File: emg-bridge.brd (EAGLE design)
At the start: 98.7 x 40.6 mm, 23 parts

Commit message: Updated parts from eagle-lib. Worked out pinouts for all connectors.
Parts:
- removed U$3: STEWART_SS-666604-NF, eagle-lib:STEWART_SS-666604-NF
- removed U$4: TE_640389-3, eagle-lib:TE_640389-3
- added J1, J2: RJ25_4X1, eagle-lib:RJ25_4X1
- U$1: value STEWART_SS-666604-NF -> M03_0.156IN-RA; device eagle-lib:STEWART_SS-666604-NF -> eagle-lib:TE_640389-3
- moved JP2 58.6 mm to (68.6, 31.8), turned to 0 degrees
- moved U$1 53.6 mm to (55.9, 15.2), turned to 180 degrees
- moved U$2 5.68 mm to (57.1, 31.8)
- moved C2 5.08 mm to (61.0, 25.4)
- moved C1 4.02 mm to (57.1, 38.1)
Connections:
- new net +VE: JP2.1, R1.2, R11.2, R13.2, R15.2, R3.2, R5.2, R7.2, R9.2, U$2.8
- new net -VE: C2.1, R10.2, R12.2, R14.2, R16.2, R2.2, R4.2, R6.2, R8.2, U$2.5
- new net CH1: J1.P$4, JP2.3
- new net CH2: J1.P$10, JP2.4
- new net CH3: J1.P$16, JP2.5
- new net CH4: J1.P$22, JP2.6
- new net CH5: J2.P$4, JP2.7
- new net CH6: J2.P$10, JP2.8
- new net CH7: J2.P$16, JP2.9
- new net CH8: J2.P$22, JP2.10
- new net GND: C2.2, J1.P$11, J1.P$14, J1.P$17, J1.P$2, J1.P$20, J1.P$23, J1.P$5, J1.P$8, J2.P$11, J2.P$14, J2.P$17, J2.P$2, J2.P$20, J2.P$23, J2.P$5, J2.P$8, JP2.2, U$1.P$2, U$2.3, U$2.6
- new net N$1: J1.P$1, R2.1
- new net N$11: J1.P$13, R6.1
- new net N$13: J1.P$15, R5.1
- new net N$16: J1.P$19, R8.1
- new net N$18: J1.P$21, R7.1
- new net N$2: C1.2, U$2.4
- new net N$21: J2.P$1, R10.1
- new net N$23: J2.P$3, R9.1
- new net N$26: J2.P$7, R12.1
- new net N$28: J2.P$9, R11.1
- new net N$3: J1.P$3, R1.1
- new net N$31: J2.P$13, R14.1
- new net N$33: J2.P$15, R13.1
- new net N$36: J2.P$19, R16.1
- new net N$38: J2.P$21, R15.1
- new net N$4: C1.1, U$2.2
- new net N$6: J1.P$7, R4.1
- new net N$8: J1.P$9, R3.1

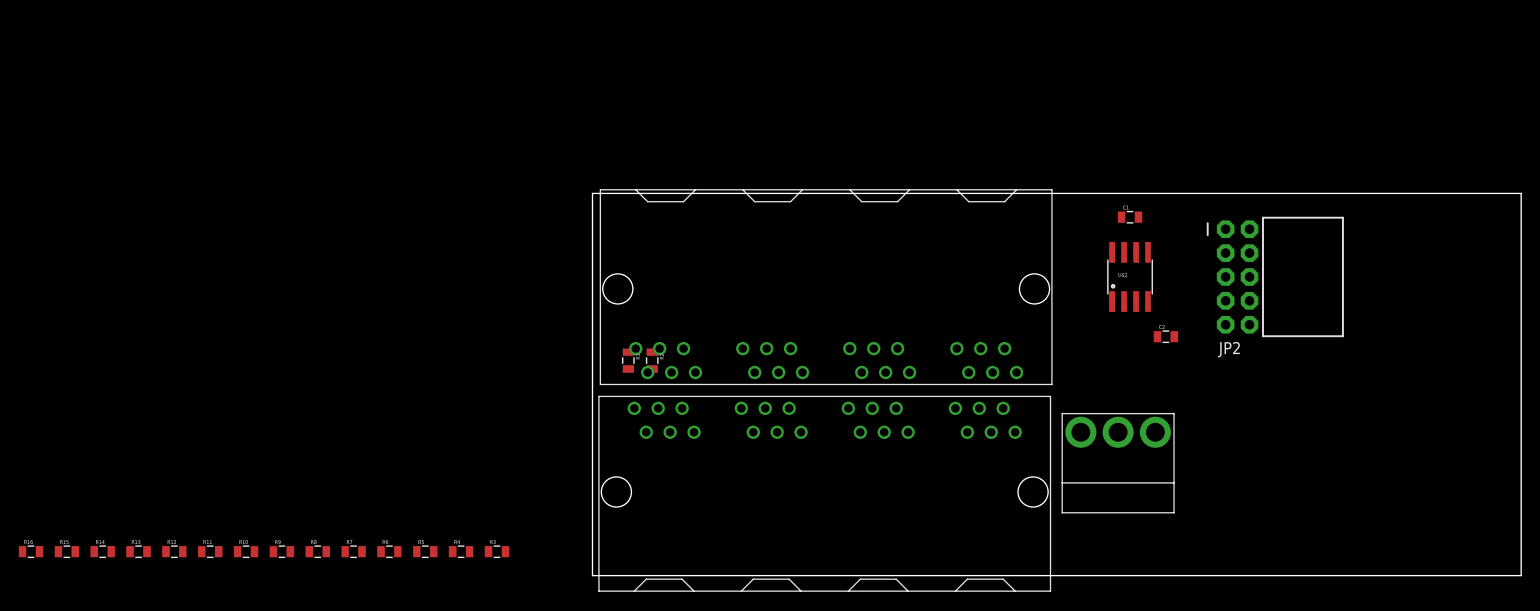
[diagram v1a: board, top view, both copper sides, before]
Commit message: Schematic cleaned up and board layout/routing rough draft completed.
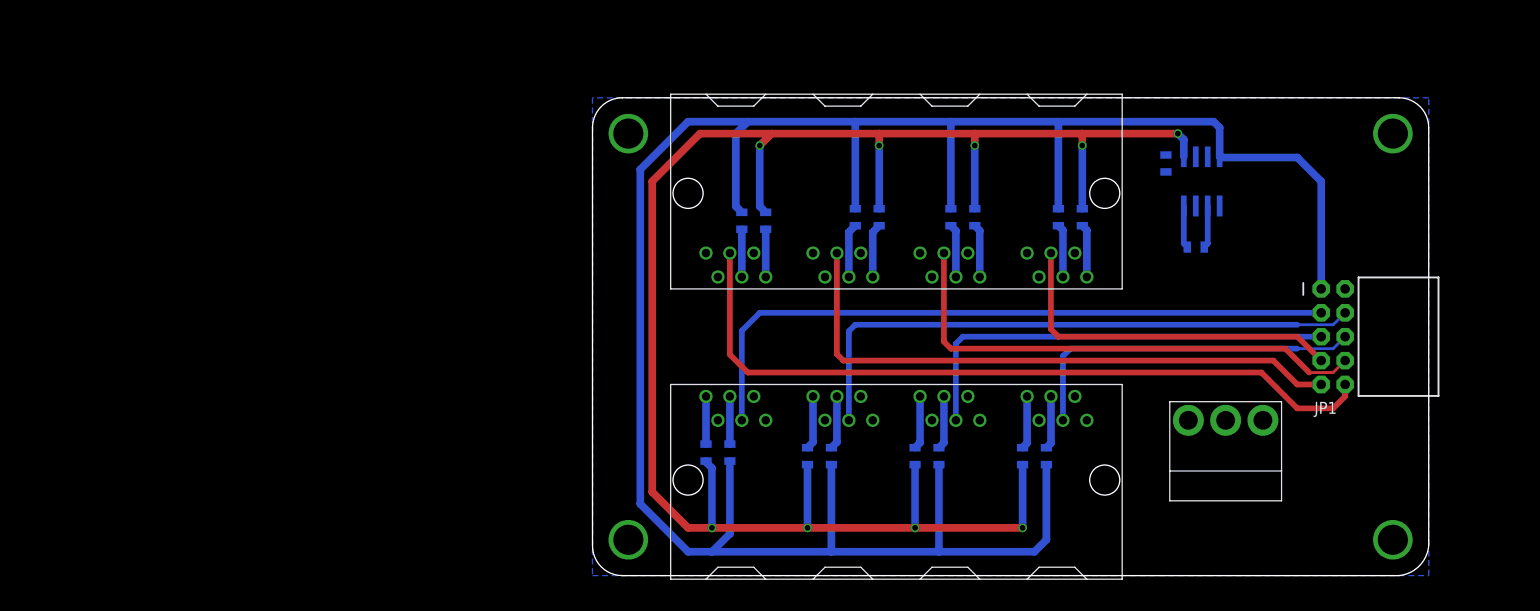
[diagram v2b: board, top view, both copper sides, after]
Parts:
- removed JP2: M05X2RAF, SparkFun-Connectors:2X5-RAF
- removed U$1: M03_0.156IN-RA, eagle-lib:TE_640389-3
- removed U$2: ADM660ARZ, eagle-lib:SOIC8
- added J3: M03_0.156IN-RA, eagle-lib:TE_640389-3
- added JP1: M05X2RAF, SparkFun-Connectors:2X5-RAF
- added U1: ADM660ARZ, eagle-lib:SOIC8
- C1, C2: value (none) -> 10uF
- R1, R10, R11, R12, R13, R14, R15, R16, R2, R3, R4, R5, R6, R7, R8, R9: value (none) -> 100
- moved R10 95.7 mm to (52.1, 38.1), flipped to the bottom, turned to 90 degrees
- moved R12 92.2 mm to (40.6, 38.1), flipped to the bottom, turned to 90 degrees
- moved R9 89.9 mm to (49.5, 38.1), flipped to the bottom, turned to 90 degrees
- moved R14 89.9 mm to (30.5, 38.1), flipped to the bottom, turned to 90 degrees
- moved R11 86.4 mm to (38.1, 38.1), flipped to the bottom, turned to 90 degrees
- moved R16 85.7 mm to (18.4, 37.7), flipped to the bottom, turned to 90 degrees
- moved R13 84.1 mm to (27.9, 38.1), flipped to the bottom, turned to 90 degrees
- moved R15 79.9 mm to (15.9, 37.7), flipped to the bottom, turned to 90 degrees
- moved R8 75.6 mm to (45.7, 12.7), flipped to the bottom, turned to 270 degrees
- moved R7 74.4 mm to (48.3, 12.7), flipped to the bottom, turned to 270 degrees
- moved J2 60.9 mm to (54.5, 40.6), turned to 180 degrees
- moved R6 56.8 mm to (34.3, 12.7), flipped to the bottom, turned to 270 degrees
- moved R5 55.5 mm to (36.8, 12.7), flipped to the bottom, turned to 270 degrees
- moved J1 42.1 mm to (10.2, 10.2), turned to 0 degrees
- moved R4 38.2 mm to (22.9, 12.7), flipped to the bottom, turned to 270 degrees
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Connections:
- net +VE: now also JP1.1, U1.8; no longer JP2.1, U$2.8
- net -VE: now also U1.5; no longer U$2.5
- net CH1: now also JP1.3; no longer JP2.3
- net CH2: now also JP1.4; no longer JP2.4
- net CH3: now also JP1.5; no longer JP2.5
- net CH4: now also JP1.6; no longer JP2.6
- net CH5: now also JP1.7; no longer JP2.7
- net CH6: now also JP1.8; no longer JP2.8
- net CH7: now also JP1.9; no longer JP2.9
- net CH8: now also JP1.10; no longer JP2.10
- net GND: now also J3.P$2, JP1.2, U1.3, U1.6; no longer JP2.2, U$1.P$2, U$2.3, U$2.6
- net N$2: now also U1.4; no longer U$2.4
- net N$4: now also U1.2; no longer U$2.2
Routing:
- net +VE: track 0.00 -> 246.9 mm
- net -VE: track 0.00 -> 195.3 mm, vias 0 -> 9
- net CH8: track 0.00 -> 80.4 mm
- net CH1: track 0.00 -> 71.9 mm
- net CH7: track 0.00 -> 63.6 mm
- net CH2: track 0.00 -> 63.0 mm
- net CH6: track 0.00 -> 54.0 mm
- net CH3: track 0.00 -> 47.3 mm
- net CH5: track 0.00 -> 38.2 mm
- net CH4: track 0.00 -> 37.7 mm
- net N$33: track 0.00 -> 5.73 mm
- net N$31: track 0.00 -> 5.73 mm
- net N$8: track 0.00 -> 5.69 mm
- net N$6: track 0.00 -> 5.69 mm
- net N$28: track 0.00 -> 5.67 mm
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- added copper zone on layer 16, net GND
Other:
- board size 98.7 x 40.6 mm -> 88.9 x 50.8 mm

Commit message: Updated for eagle-lib changes. Finished up schematic.
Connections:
- net GND: now also J3.2; no longer J3.P$2
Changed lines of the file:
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@@
 <contactref element="U1" pad="3"/>
 <contactref element="U1" pad="6"/>
-<contactref element="J3" pad="P$2"/>
+<contactref element="J3" pad="2"/>
 <contactref element="JP1" pad="2"/>
 <polygon width="0.4064" layer="16">

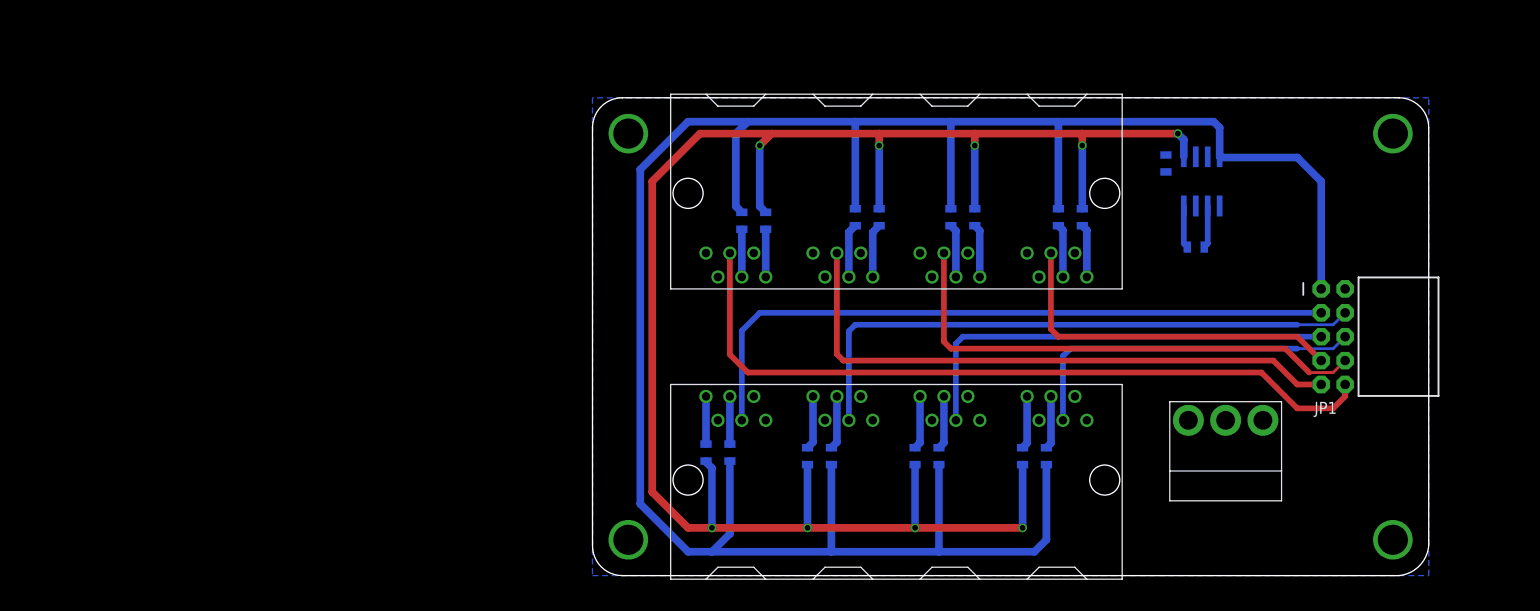
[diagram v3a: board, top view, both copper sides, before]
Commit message: Finished up layout and routing. Revision 1 complete.
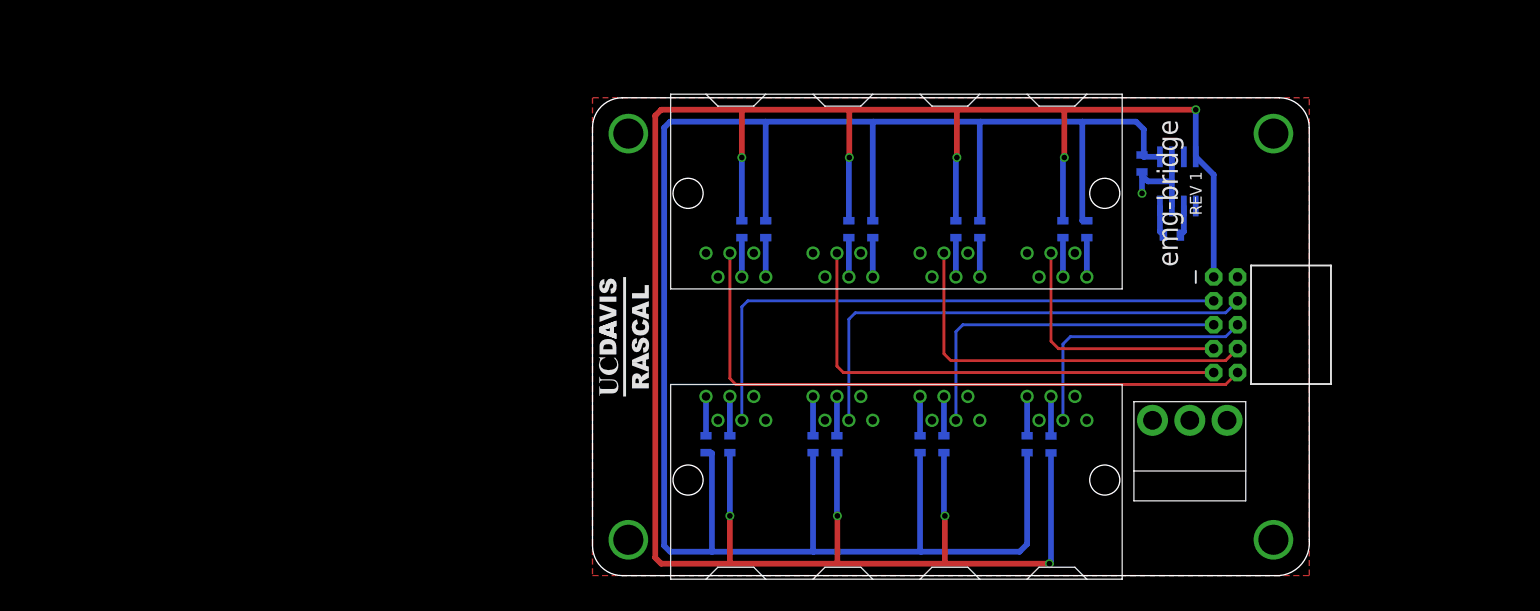
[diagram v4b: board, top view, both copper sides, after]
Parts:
- added U$1: UCDAVIS-RASCAL_LOGO-2LINE, ucdrascal-eagle-lib:UCDAVIS-RASCAL_LOGO
- moved JP1 11.5 mm to (67.3, 26.7)
- moved J3 3.81 mm to (63.5, 16.5)
- moved C1 2.84 mm to (61.6, 36.2)
- moved C2 2.54 mm to (58.4, 43.8)
- moved U1 2.54 mm to (62.2, 41.9)
- moved R13 1.44 mm to (27.3, 36.8)
- moved R14 1.44 mm to (29.8, 36.8)
- moved R3 1.40 mm to (26.0, 14.0)
- moved R4 1.40 mm to (23.4, 14.0)
- moved R11 1.38 mm to (38.6, 36.8)
- moved R12 1.38 mm to (41.2, 36.8)
- moved R5 1.38 mm to (37.4, 14.0)
- moved R6 1.38 mm to (34.8, 14.0)
- moved R10 1.36 mm to (52.6, 36.8)
- moved R9 1.36 mm to (50.0, 36.8)
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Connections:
- net CH1: now also J1.A4; no longer J1.P$4
- net CH2: now also J1.B4; no longer J1.P$10
- net CH3: now also J1.C4; no longer J1.P$16
- net CH4: now also J1.D4; no longer J1.P$22
- net CH5: now also J2.A4; no longer J2.P$4
- net CH6: now also J2.B4; no longer J2.P$10
- net CH7: now also J2.C4; no longer J2.P$16
- net CH8: now also J2.D4; no longer J2.P$22
- net GND: now also J1.A2, J1.A5, J1.B2, J1.B5, J1.C2, J1.C5, J1.D2, J1.D5, J2.A2, J2.A5, J2.B2, J2.B5, J2.C2, J2.C5, J2.D2, J2.D5; no longer J1.P$11, J1.P$14, J1.P$17, J1.P$2, J1.P$20, J1.P$23, J1.P$5, J1.P$8, J2.P$11, J2.P$14, J2.P$17, J2.P$2, J2.P$20, J2.P$23, J2.P$5, J2.P$8
- net N$1: now also J1.A1; no longer J1.P$1
- net N$11: now also J1.C1; no longer J1.P$13
- net N$13: now also J1.C3; no longer J1.P$15
- net N$16: now also J1.D1; no longer J1.P$19
- net N$18: now also J1.D3; no longer J1.P$21
- net N$21: now also J2.A1; no longer J2.P$1
- net N$23: now also J2.A3; no longer J2.P$3
- net N$26: now also J2.B1; no longer J2.P$7
- net N$28: now also J2.B3; no longer J2.P$9
- net N$3: now also J1.A3; no longer J1.P$3
- net N$31: now also J2.C1; no longer J2.P$13
- net N$33: now also J2.C3; no longer J2.P$15
- net N$36: now also J2.D1; no longer J2.P$19
- net N$38: now also J2.D3; no longer J2.P$21
- net N$6: now also J1.B1; no longer J1.P$7
- net N$8: now also J1.B3; no longer J1.P$9
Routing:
- net -VE: track 195.3 -> 224.8 mm, vias 9 -> 0
- net +VE: track 246.9 -> 260.1 mm, vias 0 -> 9
- net CH8: track 80.4 -> 68.1 mm
- net CH6: track 54.0 -> 42.7 mm
- net CH5: track 38.2 -> 27.0 mm
- net CH7: track 63.6 -> 52.4 mm
- net GND: track 0.00 -> 10.9 mm, vias 0 -> 1
- net CH4: track 37.7 -> 27.5 mm
- net CH2: track 63.0 -> 52.9 mm
- net CH3: track 47.3 -> 37.1 mm
- net CH1: track 71.9 -> 62.5 mm
- net N$33: track 5.73 -> 4.18 mm
- net N$31: track 5.73 -> 4.18 mm
- net N$8: track 5.69 -> 4.18 mm
- net N$6: track 5.69 -> 4.18 mm
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- added copper zone on layer 1, net GND
- removed copper zone on layer 16, net GND
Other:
- board size 88.9 x 50.8 mm -> 76.2 x 50.8 mm
- board text added: "REV 1"
- board text added: "emg-bridge"

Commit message: Added channel numbers on silkscreen.
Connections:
- net GND: now also J3.1, J3.3
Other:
- board text added: "CH 1"
- board text added: "CH 2"
- board text added: "CH 3"
- board text added: "CH 4"
- board text added: "CH 5"
- board text added: "CH 6"
- board text added: "CH 7"
- board text added: "CH 8"
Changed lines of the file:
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@@
 <text x="62.23" y="40.64" size="2.1844" layer="21" font="vector" ratio="15" rot="R90" align="bottom-center">emg-bridge</text>
 <text x="64.77" y="40.64" size="1.27" layer="21" font="vector" ratio="10" rot="R90" align="bottom-center">REV 1</text>
+<text x="14.605" y="20.955" size="1.016" layer="21" font="vector" ratio="10" rot="R90" align="center-left">CH 1</text>
+<text x="26.035" y="20.955" size="1.016" layer="21" font="vector" ratio="10" rot="R90" align="center-left">CH 2</text>
+<text x="37.465" y="20.955" size="1.016" layer="21" font="vector" ratio="10" rot="R90" align="center-left">CH 3</text>
+<text x="48.895" y="20.955" size="1.016" layer="21" font="vector" ratio="10" rot="R90" align="center-left">CH 4</text>
+<text x="14.605" y="29.845" size="1.016" layer="21" font="vector" ratio="10" rot="R270" align="center-left">CH 8</text>
+<text x="26.035" y="29.845" size="1.016" layer="21" font="vector" ratio="10" rot="R270" align="center-left">CH 7</text>
+<text x="37.465" y="29.845" size="1.016" layer="21" font="vector" ratio="10" rot="R270" align="center-left">CH 6</text>
+<text x="48.895" y="29.845" size="1.016" layer="21" font="vector" ratio="10" rot="R270" align="center-left">CH 5</text>
+<wire x1="12.7" y1="25.4" x2="50.8" y2="25.4" width="0.127" layer="21"/>
 </plain>
 <attributes>
@@
 <wire x1="58.42" y1="42.545" x2="58.42" y2="40.64" width="0.6096" layer="16"/>
 <via x="58.42" y="40.64" extent="1-16" drill="0.6"/>
+<contactref element="J3" pad="3"/>
+<contactref element="J3" pad="1"/>
 </signal>
 <signal name="CH1">
